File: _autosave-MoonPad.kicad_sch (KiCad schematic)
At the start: 56 parts, among them IC1 W25Q16JVUXIQ, J1 OLED, J3 USB-C 2.0 Receptacle, SW1 Reset, U3 RP2040, U4 Hall_Sensor, U5 Hall_Sensor, U6 AP2112K-3.3, Y1 JGHC S3212000181080

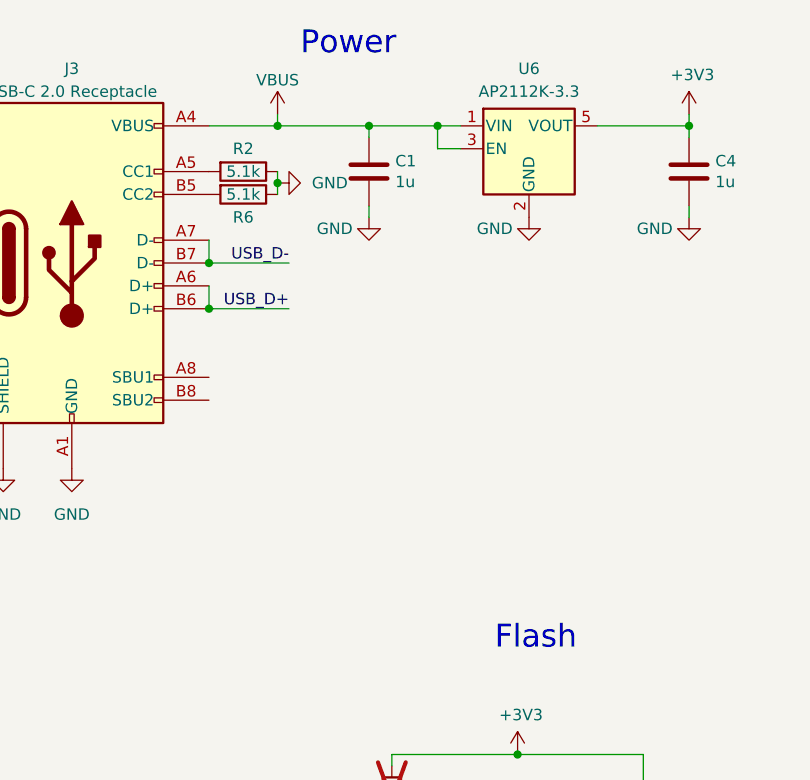
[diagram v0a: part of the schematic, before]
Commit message: Added ESD Protection
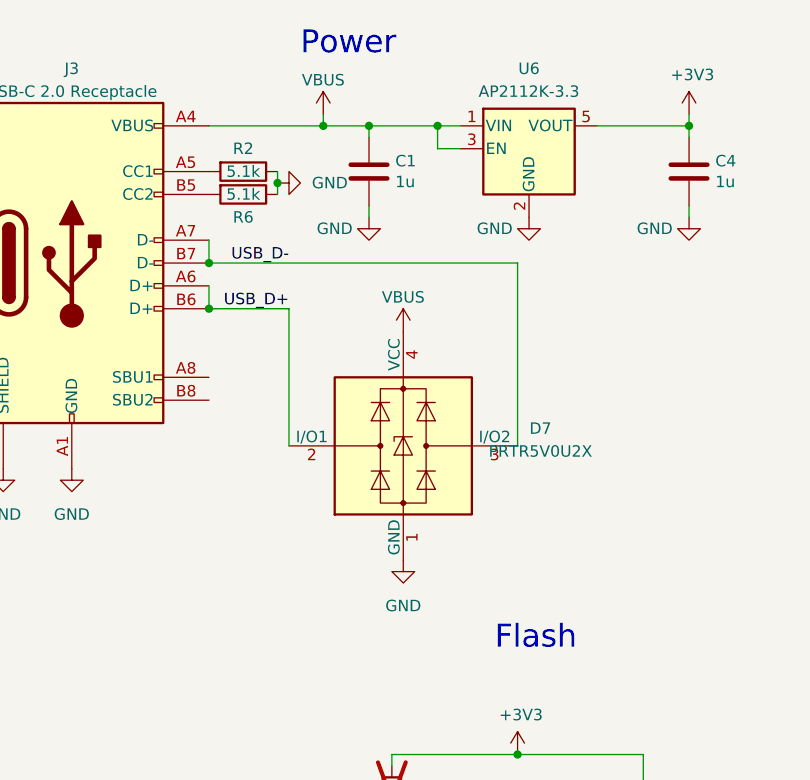
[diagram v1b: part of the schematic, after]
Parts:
- added D7: PRTR5V0U2X, Package_TO_SOT_SMD:SOT-143, symbol Power_Protection:PRTR5V0U2X
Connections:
- net GND: now also D7.1 (GND)
- net USB_D+: now also D7.2 (I/O1)
- net USB_D-: now also D7.3 (I/O2)
- net VBUS: now also D7.4 (VCC)
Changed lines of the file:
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@@
   (junction (at 207.01 81.28) (diameter 0) (color 0 0 0 0)
   )
-  (junction (at 57.15 35.56) (diameter 0) (color 0 0 0 0)
+  (junction (at 62.23 35.56) (diameter 0) (color 0 0 0 0)
   )
   (junction (at 355.6 160.02) (diameter 0) (color 0 0 0 0)
@@
     (stroke (width 0) (type default))
   )
-  (wire (pts (xy 57.15 34.29) (xy 57.15 35.56))
+  (wire (pts (xy 62.23 34.29) (xy 62.23 35.56))
     (stroke (width 0) (type default))
   )
@@
     (stroke (width 0) (type default))
   )
+  (wire (pts (xy 83.82 50.8) (xy 83.82 71.12))
+    (stroke (width 0) (type default))
+  )
   (wire (pts (xy 168.91 60.96) (xy 177.8 60.96))
     (stroke (width 0) (type default))
@@
     (stroke (width 0) (type default))
   )
+  (wire (pts (xy 49.53 35.56) (xy 62.23 35.56))
+    (stroke (width 0) (type default))
+  )
   (wire (pts (xy 204.47 81.28) (xy 207.01 81.28))
     (stroke (width 0) (type default))
@@
     (stroke (width 0) (type default))
   )
-  (wire (pts (xy 57.15 35.56) (xy 67.31 35.56))
+  (wire (pts (xy 62.23 35.56) (xy 67.31 35.56))
     (stroke (width 0) (type default))
   )
@@
     (stroke (width 0) (type default))
   )
-  (wire (pts (xy 49.53 50.8) (xy 58.42 50.8))
+  (wire (pts (xy 49.53 50.8) (xy 83.82 50.8))
     (stroke (width 0) (type default))
   )
@@
     (stroke (width 0) (type default))
   )
+  (wire (pts (xy 58.42 55.88) (xy 58.42 71.12))
+    (stroke (width 0) (type default))
+  )
   (wire (pts (xy 269.24 62.23) (xy 269.24 60.96))
     (stroke (width 0) (type default))
@@
     (stroke (width 0) (type default))
   )
-  (wire (pts (xy 49.53 35.56) (xy 57.15 35.56))
-    (stroke (width 0) (type default))
-  )
   (wire (pts (xy 229.87 101.6) (xy 236.22 101.6))
     (stroke (width 0) (type default))
@@
     )
   )
-  (symbol (lib_id "power:VBUS") (at 57.15 34.29 0) (unit 1)
+  (symbol (lib_id "power:VBUS") (at 62.23 34.29 0) (unit 1)
     (in_bom yes) (on_board yes) (dnp no)
-    (property "Reference" "#PWR03" (at 57.15 38.1 0)
+    (property "Reference" "#PWR03" (at 62.23 38.1 0)
       (effects (font (size 1.27 1.27)) hide)
     )
-    (property "Value" "VBUS" (at 57.15 30.48 0)
+    (property "Value" "VBUS" (at 62.23 30.48 0)
       (effects (font (size 1.27 1.27)))
     )
-    (property "Footprint" "" (at 57.15 34.29 0)
+    (property "Footprint" "" (at 62.23 34.29 0)
       (effects (font (size 1.27 1.27)) hide)
     )
-    (property "Datasheet" "" (at 57.15 34.29 0)
+    (property "Datasheet" "" (at 62.23 34.29 0)
       (effects (font (size 1.27 1.27)) hide)
     )
@@
     )
   )
+  (symbol (lib_id "power:GND") (at 71.12 83.82 0) (unit 1)
+    (in_bom yes) (on_board yes) (dnp no) (fields_autoplaced)
+    (property "Reference" "#PWR047" (at 71.12 90.17 0)
+      (effects (font (size 1.27 1.27)) hide)
+    )
+    (property "Value" "GND" (at 71.12 88.9 0)
+      (effects (font (size 1.27 1.27)))
+    )
+    (property "Footprint" "" (at 71.12 83.82 0)
+      (effects (font (size 1.27 1.27)) hide)
+    )
+    (property "Datasheet" "" (at 71.12 83.82 0)
+      (effects (font (size 1.27 1.27)) hide)
+    )
+    (pin "1")
+    (instances
+      (project "MoonPad"
+        (path "/66a337f3-0e1a-4778-bb9f-853ccc5d3181"
+          (reference "#PWR047") (unit 1)
+        )
+      )
+    )
+  )
   (symbol (lib_id "power:GND") (at 69.85 124.46 0) (unit 1)
     (in_bom yes) (on_board yes) (dnp no)
@@
     )
   )
+  (symbol (lib_id "Power_Protection:PRTR5V0U2X") (at 71.12 71.12 0) (unit 1)
+    (in_bom yes) (on_board yes) (dnp no) (fields_autoplaced)
+    (property "Reference" "D7" (at 86.36 69.1897 0)
+      (effects (font (size 1.27 1.27)))
+    )
+    (property "Value" "PRTR5V0U2X" (at 86.36 71.7297 0)
+      (effects (font (size 1.27 1.27)))
+    )
+    (property "Footprint" "Package_TO_SOT_SMD:SOT-143" (at 72.644 71.12 0)
+      (effects (font (size 1.27 1.27)) hide)
+    )
+    (property "Datasheet" "https://assets.nexperia.com/documents/data-sheet/PRTR5V0U2X.pdf" (at 72.644 71.12 0)
+      (effects (font (size 1.27 1.27)) hide)
+    )
+    (pin "1")
+    (pin "2")
+    (pin "3")
+    (pin "4")
+    (instances
+      (project "MoonPad"
+        (path "/66a337f3-0e1a-4778-bb9f-853ccc5d3181"
+          (reference "D7") (unit 1)
+        )
+      )
+    )
+  )
   (symbol (lib_id "Device:R") (at 59.69 116.84 270) (unit 1)
     (in_bom yes) (on_board yes) (dnp no)
@@
         )
       )
+    )
+  )
+  (symbol (lib_id "power:VBUS") (at 71.12 58.42 0) (unit 1)
+    (in_bom yes) (on_board yes) (dnp no)
+    (property "Reference" "#PWR048" (at 71.12 62.23 0)
+      (effects (font (size 1.27 1.27)) hide)
+    )
+    (property "Value" "VBUS" (at 71.12 54.61 0)
+      (effects (font (size 1.27 1.27)))
+    )
+    (property "Footprint" "" (at 71.12 58.42 0)
+      (effects (font (size 1.27 1.27)) hide)
+    )
+    (property "Datasheet" "" (at 71.12 58.42 0)
+      (effects (font (size 1.27 1.27)) hide)
+    )
+    (pin "1")
+    (instances
+      (project "MoonPad"
+        (path "/66a337f3-0e1a-4778-bb9f-853ccc5d3181"
+          (reference "#PWR048") (unit 1)
+        )
+      )
